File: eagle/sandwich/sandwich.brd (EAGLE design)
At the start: 100 x 81.3 mm, 128 parts, among them IC1 ATMEGA644-20PU, J1 AVR_SPI_PRG_6NS, Q1 20MHZ, Q2 IRFZ44N, Q3 IRFZ44N, T0 4.7k, T1 4.7k, T2 4.7k, T3 4.7k, T4 2N2222

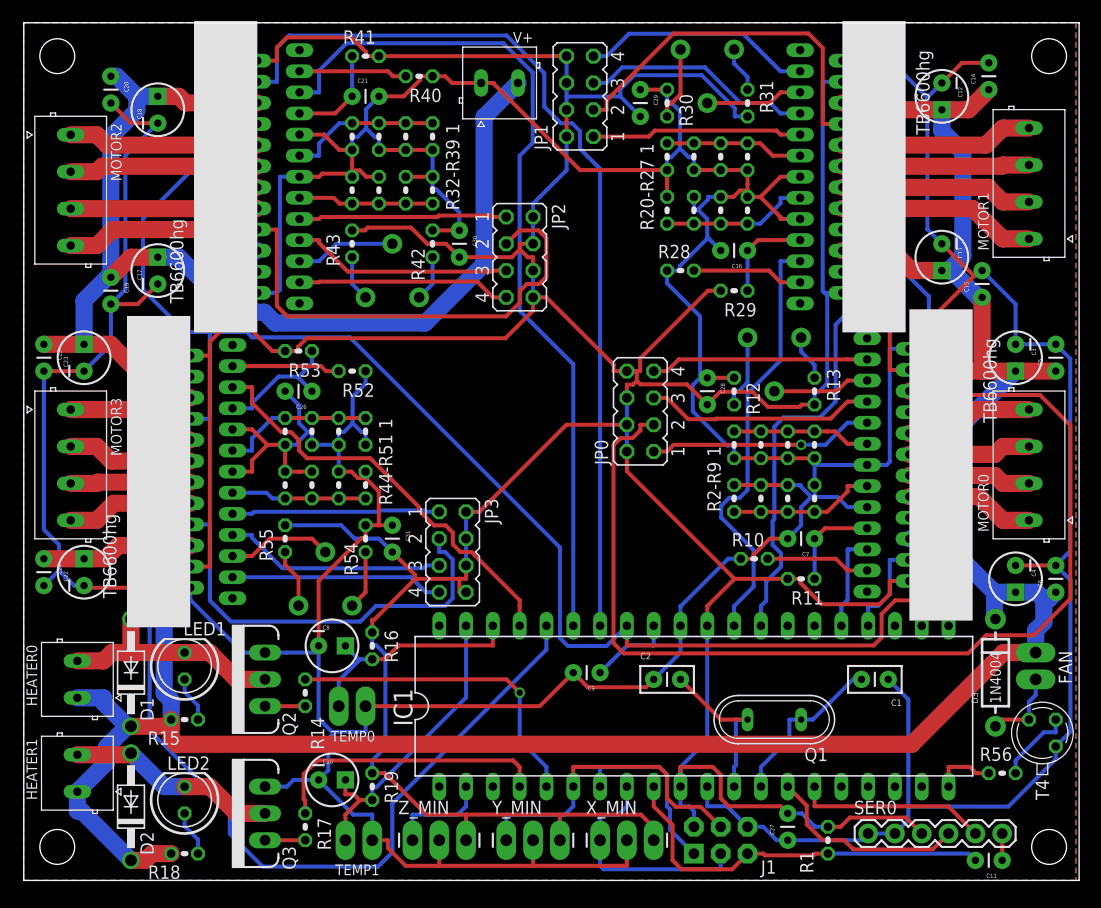
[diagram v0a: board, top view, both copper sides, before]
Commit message: beefed up some traces
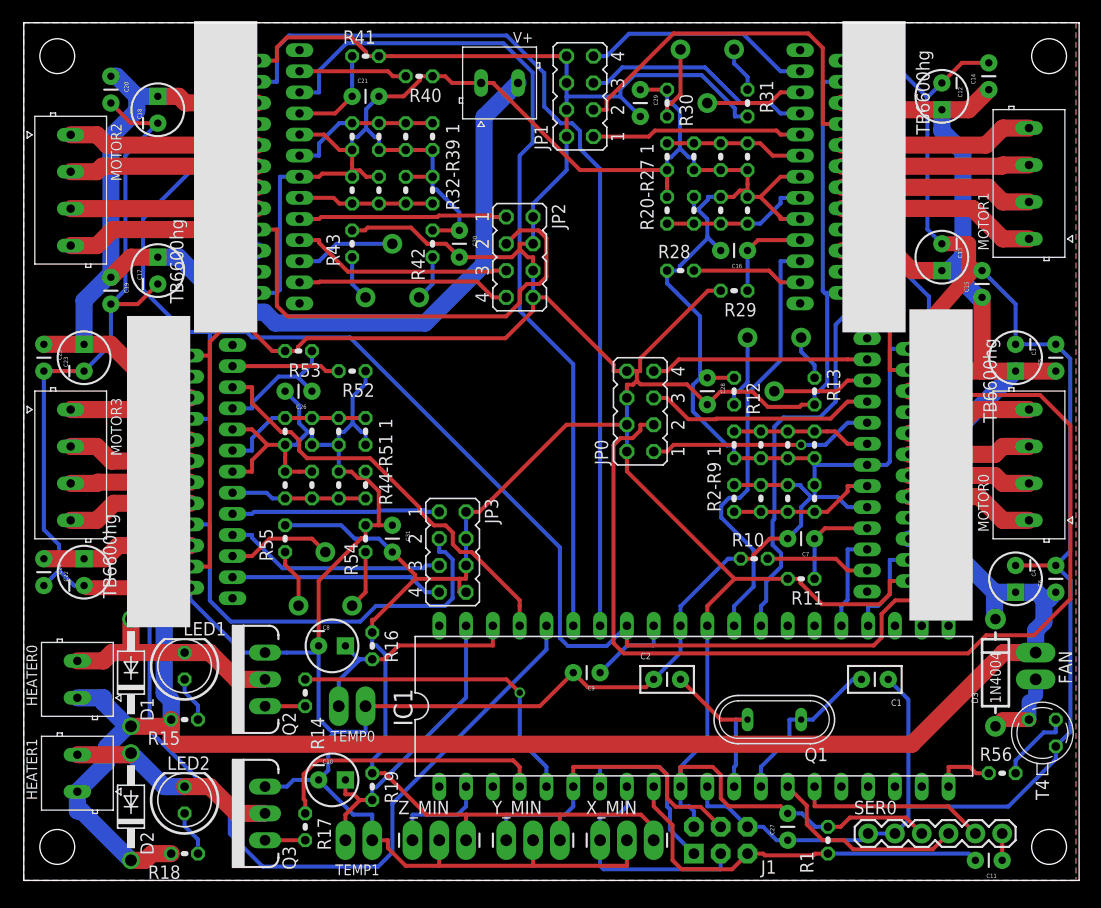
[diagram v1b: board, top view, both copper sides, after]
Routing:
- net GND: track 648.3 -> 649.7 mm
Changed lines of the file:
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@@
 <wire x1="43.335" y1="75.565" x2="40.5766" y2="75.565" width="0.381" layer="1"/>
 <wire x1="40.5766" y1="75.565" x2="39.9416" y2="76.2" width="0.381" layer="1"/>
-<wire x1="15.78" y1="27.735" x2="5.92" y2="27.735" width="0.381" layer="1"/>
+<wire x1="15.78" y1="27.735" x2="5.92" y2="27.735" width="1.4224" layer="1"/>
 <wire x1="5.92" y1="27.735" x2="5.715" y2="27.94" width="0.381" layer="1"/>
 <wire x1="66.04" y1="64.77" x2="67.2466" y2="64.77" width="0.381" layer="1"/>
@@
 <wire x1="99.1618" y1="49.4282" x2="99.1618" y2="31.2168" width="0.381" layer="16"/>
 <wire x1="99.1618" y1="31.2168" x2="97.79" y2="29.845" width="0.381" layer="16"/>
-<wire x1="90.0426" y1="57.2774" x2="90.5502" y2="57.785" width="0.381" layer="1"/>
+<wire x1="90.0426" y1="57.9124" x2="90.5502" y2="57.785" width="0.381" layer="1"/>
 <wire x1="90.5502" y1="57.785" x2="90.805" y2="57.785" width="0.381" layer="1"/>
-<wire x1="85.7692" y1="50.37" x2="85.7692" y2="53.004" width="0.381" layer="1"/>
-<wire x1="85.7692" y1="53.004" x2="90.0426" y2="57.2774" width="0.381" layer="1"/>
-<wire x1="90.0426" y1="57.2774" x2="86.995" y2="60.325" width="0.381" layer="1"/>
-<wire x1="83.915" y1="50.37" x2="85.7692" y2="50.37" width="0.381" layer="1"/>
+<wire x1="85.7692" y1="50.37" x2="85.7692" y2="53.004" width="1.4224" layer="1"/>
+<wire x1="85.7692" y1="53.004" x2="90.0426" y2="57.9124" width="1.4224" layer="1"/>
+<wire x1="90.0426" y1="57.9124" x2="89.535" y2="57.9124" width="1.4224" layer="1"/>
+<wire x1="89.535" y1="57.9124" x2="89.535" y2="60.325" width="1.4224" layer="1"/>
+<wire x1="89.535" y1="60.325" x2="86.995" y2="60.325" width="1.4224" layer="1"/>
+<wire x1="83.915" y1="50.37" x2="85.7692" y2="50.37" width="1.4224" layer="1"/>
 <wire x1="85.6229" y1="74.1929" x2="86.995" y2="75.565" width="0.381" layer="16"/>
 <wire x1="86.995" y1="60.325" x2="85.6229" y2="61.6971" width="0.381" layer="16"/>
@@
 <contactref element="D3" pad="A"/>
 <contactref element="T4" pad="3"/>
-<wire x1="95.885" y1="19.05" x2="95.885" y2="17.564" width="0.381" layer="16"/>
+<wire x1="95.885" y1="19.05" x2="95.885" y2="17.564" width="1.4224" layer="16"/>
 <wire x1="95.885" y1="17.564" x2="95.25" y2="16.929" width="0.381" layer="16"/>
-<wire x1="95.25" y1="16.929" x2="95.25" y2="15.24" width="0.381" layer="16"/>
-<wire x1="95.25" y1="15.24" x2="92.71" y2="15.24" width="0.381" layer="1"/>
+<wire x1="95.25" y1="16.929" x2="95.25" y2="15.24" width="1.4224" layer="16"/>
+<wire x1="95.25" y1="15.24" x2="92.71" y2="15.24" width="1.4224" layer="1"/>
 <wire x1="92.71" y1="15.24" x2="92.075" y2="14.605" width="0.381" layer="1"/>
 </signal>

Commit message: added AMT and Open HW logos
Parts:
- added U$9: (no value), ohw-logo:OSHW_10X200_NOTEXT
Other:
- board text added: "acemonstertoys.org"
- board text added: "github.com/atom-bomb/sandwich"
- board text added: "open hw"

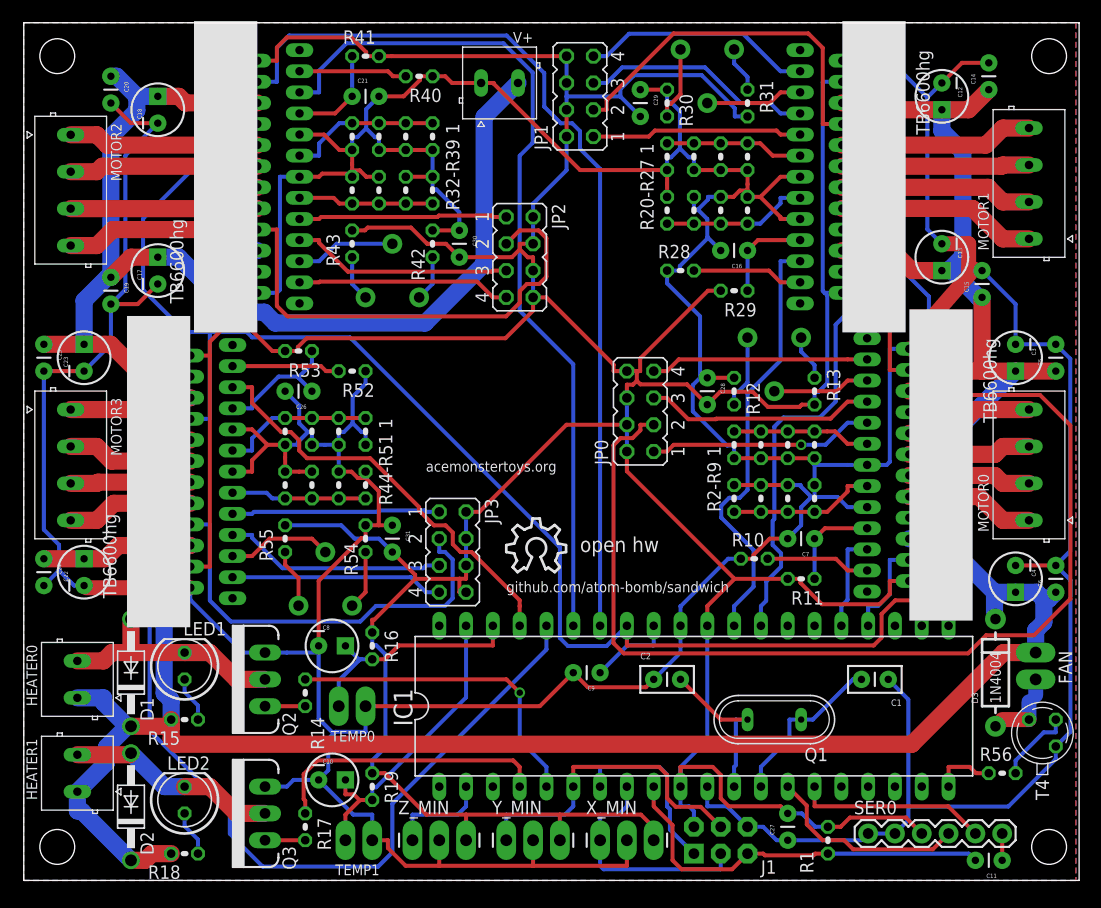
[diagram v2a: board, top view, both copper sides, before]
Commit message: Fatten up a few ground traces...just in case.
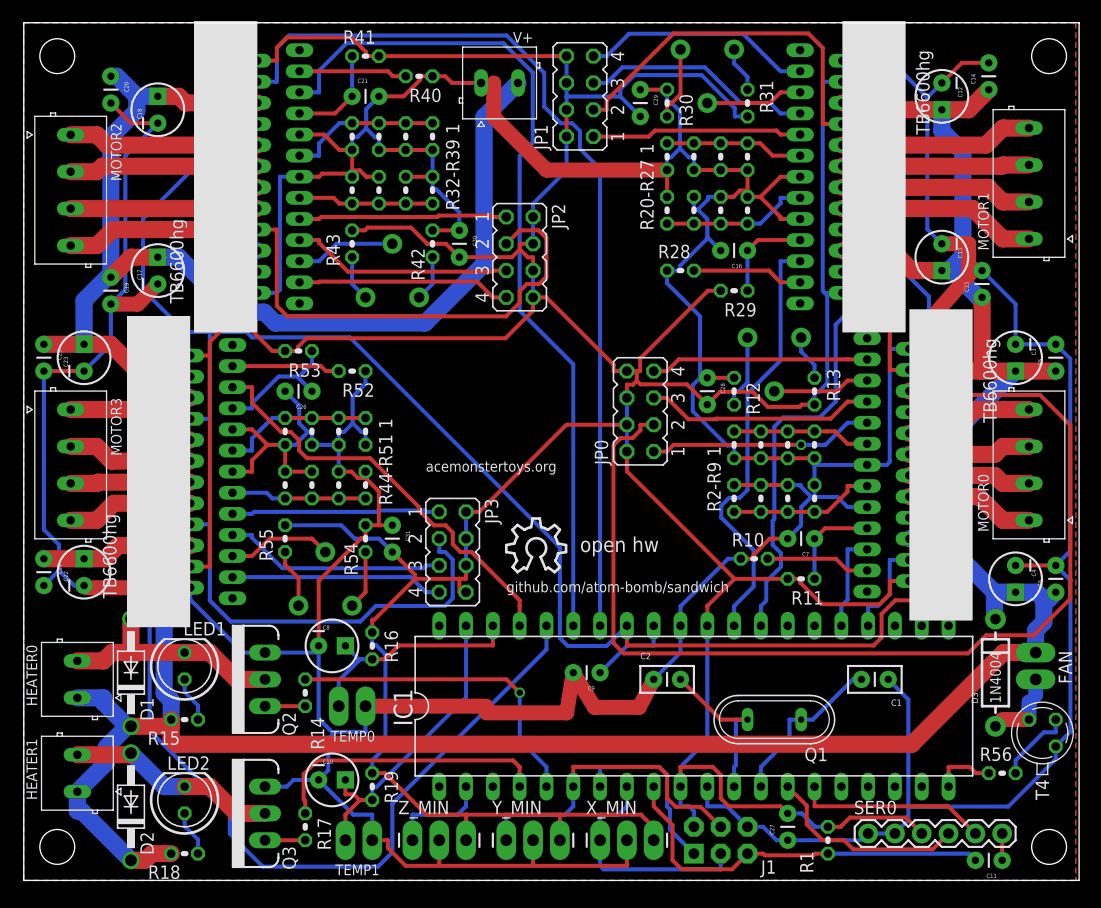
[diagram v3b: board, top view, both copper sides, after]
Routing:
- net GND: track 649.7 -> 656.7 mm
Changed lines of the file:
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@@
 <wire x1="29.3554" y1="13.917" x2="27.94" y2="15.3323" width="0.381" layer="16"/>
 <wire x1="27.94" y1="15.3323" x2="27.94" y2="21.59" width="0.381" layer="16"/>
-<wire x1="27.94" y1="21.59" x2="24.9302" y2="21.59" width="0.381" layer="16"/>
-<wire x1="22.86" y1="21.59" x2="24.9302" y2="21.59" width="0.381" layer="16"/>
+<wire x1="27.94" y1="21.59" x2="22.86" y2="21.59" width="0.381" layer="16"/>
 <wire x1="32.385" y1="14.0842" x2="29.5226" y2="14.0842" width="0.381" layer="16"/>
 <wire x1="29.5226" y1="14.0842" x2="29.3554" y2="13.917" width="0.381" layer="16"/>
@@
 <wire x1="63.0135" y1="68.5166" x2="62.1742" y2="69.3559" width="0.381" layer="16"/>
 <wire x1="63.5" y1="67.31" x2="63.5" y2="68.5166" width="0.381" layer="16"/>
-<wire x1="60.96" y1="67.31" x2="60.96" y2="65.9766" width="0.381" layer="1"/>
-<wire x1="44.5352" y1="75.565" x2="44.5352" y2="75.49" width="0.381" layer="1"/>
-<wire x1="44.5352" y1="75.49" x2="52.7152" y2="67.31" width="0.381" layer="1"/>
-<wire x1="52.7152" y1="67.31" x2="60.96" y2="67.31" width="0.381" layer="1"/>
-<wire x1="60.96" y1="64.77" x2="60.96" y2="65.9766" width="0.381" layer="1"/>
+<wire x1="60.96" y1="67.31" x2="60.96" y2="64.77" width="0.381" layer="1"/>
+<wire x1="44.5352" y1="75.565" x2="44.5352" y2="72.315" width="1.4224" layer="1"/>
+<wire x1="44.5352" y1="72.315" x2="49.5402" y2="67.31" width="1.4224" layer="1"/>
+<wire x1="49.5402" y1="67.31" x2="60.96" y2="67.31" width="1.4224" layer="1"/>
 <wire x1="63.8749" y1="63.5634" x2="63.5" y2="63.5634" width="0.381" layer="16"/>
 <wire x1="63.8749" y1="63.5634" x2="64.8334" y2="64.5219" width="0.381" layer="16"/>
@@
 <wire x1="30.3243" y1="42.4816" x2="31.1661" y2="43.3234" width="0.381" layer="16"/>
 <wire x1="29.845" y1="41.275" x2="29.845" y2="42.4816" width="0.381" layer="16"/>
-<wire x1="28.5116" y1="41.275" x2="29.845" y2="41.275" width="0.381" layer="16"/>
+<wire x1="27.305" y1="41.275" x2="29.845" y2="41.275" width="0.381" layer="16"/>
 <wire x1="32.385" y1="16.51" x2="32.385" y2="14.0842" width="0.381" layer="16"/>
 <wire x1="27.94" y1="9.525" x2="31.2292" y2="6.2358" width="0.381" layer="16"/>
@@
 <wire x1="68.58" y1="65.3733" x2="67.8499" y2="65.3733" width="0.381" layer="1"/>
 <wire x1="67.8499" y1="65.3733" x2="67.2466" y2="64.77" width="0.381" layer="1"/>
-<wire x1="68.58" y1="65.3733" x2="68.58" y2="65.9766" width="0.381" layer="1"/>
 <wire x1="68.58" y1="64.77" x2="68.58" y2="65.3733" width="0.381" layer="1"/>
 <wire x1="63.5" y1="64.77" x2="63.5" y2="63.5634" width="0.381" layer="16"/>
@@
 <wire x1="74.93" y1="39.37" x2="74.93" y2="37.465" width="0.381" layer="16"/>
 <wire x1="74.93" y1="40.005" x2="74.93" y2="39.37" width="0.381" layer="16"/>
-<wire x1="74.93" y1="39.37" x2="78.0608" y2="39.37" width="0.381" layer="16"/>
-<wire x1="79.915" y1="39.37" x2="78.0608" y2="39.37" width="0.381" layer="16"/>
+<wire x1="74.93" y1="39.37" x2="79.915" y2="39.37" width="0.381" layer="16"/>
 <wire x1="69.7962" y1="64.7604" x2="69.7866" y2="64.77" width="0.381" layer="1"/>
 <wire x1="71.7108" y1="62.675" x2="71.7108" y2="62.8458" width="0.381" layer="1"/>
@@
 <wire x1="69.7962" y1="64.7604" x2="71.7108" y2="66.675" width="0.381" layer="1"/>
 <wire x1="73.565" y1="66.675" x2="71.7108" y2="66.675" width="0.381" layer="1"/>
-<wire x1="68.58" y1="67.31" x2="68.58" y2="65.9766" width="0.381" layer="1"/>
+<wire x1="68.58" y1="67.31" x2="68.58" y2="65.3733" width="0.381" layer="1"/>
 <wire x1="66.04" y1="67.31" x2="68.58" y2="67.31" width="0.381" layer="1"/>
 <wire x1="67.945" y1="30.48" x2="66.7384" y2="30.48" width="0.381" layer="16"/>
@@
 <wire x1="31.115" y1="67.2783" x2="31.8451" y2="67.2783" width="0.381" layer="1"/>
 <wire x1="31.8451" y1="67.2783" x2="32.4484" y2="66.675" width="0.381" layer="1"/>
-<wire x1="31.115" y1="67.2783" x2="31.115" y2="67.8816" width="0.381" layer="1"/>
-<wire x1="31.115" y1="69.215" x2="31.115" y2="67.8816" width="0.381" layer="1"/>
+<wire x1="31.115" y1="69.215" x2="31.115" y2="67.2783" width="0.381" layer="1"/>
 <wire x1="32.385" y1="33.655" x2="32.385" y2="32.4484" width="0.381" layer="1"/>
 <wire x1="27.94" y1="22.225" x2="27.94" y2="28.3764" width="0.381" layer="1"/>
 <wire x1="27.94" y1="28.3764" x2="32.012" y2="32.4484" width="0.381" layer="1"/>
 <wire x1="32.012" y1="32.4484" x2="32.385" y2="32.4484" width="0.381" layer="1"/>
-<wire x1="24.765" y1="38.735" x2="26.0984" y2="38.735" width="0.381" layer="1"/>
-<wire x1="27.305" y1="38.735" x2="26.0984" y2="38.735" width="0.381" layer="1"/>
-<wire x1="24.765" y1="38.735" x2="24.765" y2="40.0684" width="0.381" layer="1"/>
+<wire x1="24.765" y1="38.735" x2="27.305" y2="38.735" width="0.381" layer="1"/>
+<wire x1="24.765" y1="38.735" x2="24.765" y2="41.275" width="0.381" layer="1"/>
 <wire x1="29.845" y1="38.735" x2="29.845" y2="41.275" width="0.381" layer="16"/>
-<wire x1="27.305" y1="41.275" x2="28.5116" y2="41.275" width="0.381" layer="16"/>
 <wire x1="26.9278" y1="42.4816" x2="26.0984" y2="43.311" width="0.381" layer="16"/>
 <wire x1="26.0984" y1="43.311" x2="26.0984" y2="45.0216" width="0.381" layer="16"/>
@@
 <wire x1="24.765" y1="41.275" x2="25.9716" y2="41.275" width="0.381" layer="16"/>
 <wire x1="27.305" y1="41.275" x2="27.305" y2="42.4816" width="0.381" layer="16"/>
-<wire x1="24.765" y1="41.275" x2="24.765" y2="40.0684" width="0.381" layer="1"/>
 <wire x1="23.0942" y1="41.275" x2="24.765" y2="41.275" width="0.381" layer="1"/>
 <wire x1="21.6342" y1="42.735" x2="23.0942" y2="41.275" width="0.381" layer="1"/>
@@
 <wire x1="21.6342" y1="39.815" x2="21.6342" y2="38.735" width="0.381" layer="1"/>
 <wire x1="19.78" y1="38.735" x2="21.6342" y2="38.735" width="0.381" layer="1"/>
-<wire x1="8.255" y1="54.61" x2="10.795" y2="54.61" width="0.381" layer="1"/>
-<wire x1="10.795" y1="54.61" x2="12.7" y2="56.515" width="0.381" layer="1"/>
+<wire x1="8.255" y1="54.61" x2="10.795" y2="54.61" width="1.4224" layer="1"/>
+<wire x1="10.795" y1="54.61" x2="12.7" y2="56.515" width="1.4224" layer="1"/>
 <wire x1="72.39" y1="40.005" x2="74.93" y2="40.005" width="0.381" layer="1"/>
-<wire x1="52.07" y1="19.685" x2="53.4477" y2="18.3073" width="0.381" layer="1"/>
-<wire x1="53.4477" y1="18.3073" x2="58.9473" y2="18.3073" width="0.381" layer="1"/>
-<wire x1="58.9473" y1="18.3073" x2="59.69" y2="19.05" width="0.381" layer="1"/>
-<wire x1="32.385" y1="16.51" x2="48.895" y2="16.51" width="0.381" layer="1"/>
-<wire x1="48.895" y1="16.51" x2="52.07" y2="19.685" width="0.381" layer="1"/>
+<wire x1="52.07" y1="19.685" x2="54.0827" y2="16.4023" width="1.4224" layer="1"/>
+<wire x1="54.0827" y1="16.4023" x2="58.3123" y2="16.4023" width="1.4224" layer="1"/>
+<wire x1="58.3123" y1="16.4023" x2="59.69" y2="19.05" width="1.4224" layer="1"/>
+<wire x1="32.385" y1="16.51" x2="43.815" y2="16.51" width="1.4224" layer="1"/>
+<wire x1="43.815" y1="16.51" x2="43.815" y2="15.875" width="0.381" layer="1"/>
+<wire x1="43.815" y1="15.875" x2="51.435" y2="15.875" width="1.4224" layer="1"/>
+<wire x1="51.435" y1="15.875" x2="52.07" y2="19.685" width="1.4224" layer="1"/>
 <wire x1="33.02" y1="3.81" x2="33.02" y2="6.2358" width="0.381" layer="16"/>
 <wire x1="68.58" y1="5.08" x2="70.066" y2="5.08" width="0.381" layer="16"/>
